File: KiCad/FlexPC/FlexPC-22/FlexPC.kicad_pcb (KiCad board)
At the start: 2 copper layers, 12.7 x 16.6 mm, 3 parts, among them J1 Conn_01x22, J2 Conn_01x20, J3 Conn_01x14

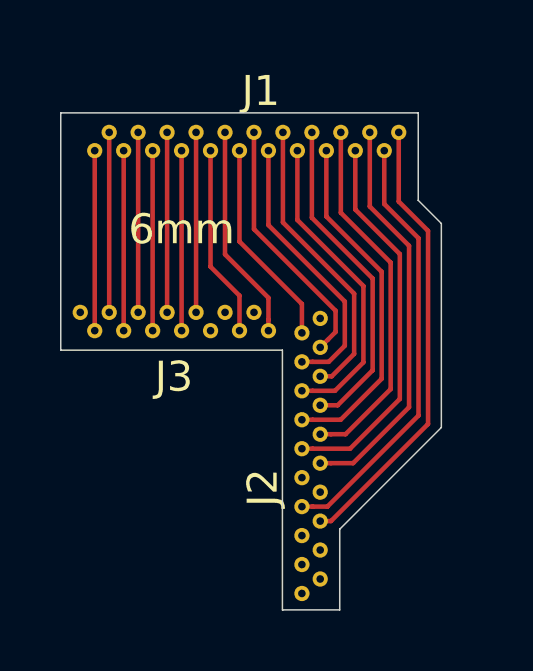
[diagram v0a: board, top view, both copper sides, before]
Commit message: WF Release Board & FlexPC's Updates
1. 23-pin and 3-pin FlexPCs' holes have teardrop shapes now
2. 23-pin flexPC tracks still need to be cleaned up. Not sure how to ensure no curved near the bending area yet.
3. WF board copper planes have been reduced to be 12.5 mils away from the edge cut.
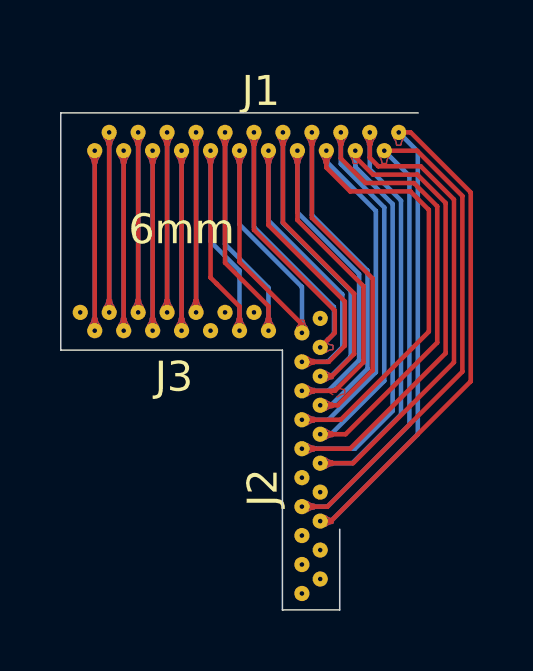
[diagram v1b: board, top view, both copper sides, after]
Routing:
- net /LINE_VALID: track 15.1 -> 31.3 mm
- net /FRAME_VALID: track 14.4 -> 30.5 mm
- net /img_d6: track 13.4 -> 28.7 mm
- net /img_d7: track 12.8 -> 27.7 mm
- net /img_d5: track 12.2 -> 26.2 mm
- net /img_d4: track 11.6 -> 25.3 mm
- net /CLK_OUT: track 11.0 -> 21.7 mm
- net /img_d3: track 10.4 -> 20.6 mm
- net /img_d1: track 9.81 -> 19.5 mm
- net /img_d2: track 9.21 -> 18.3 mm
- net /img_d0: track 8.51 -> 16.9 mm
- net /GND: track 7.21 -> 14.4 mm
- net /1V8: track 6.94 -> 13.9 mm
- net /SS_N: track 6.40 -> 12.8 mm
- net /3V3: track 6.00 -> 12.0 mm
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- added copper zone on B.Cu, net (none)
- added copper zone on F.Cu, net (none)
- added copper zone on B.Cu, net /1V8
- added copper zone on F.Cu, net /1V8
- added copper zone on B.Cu, net /3V3
- added copper zone on F.Cu, net /3V3
- added copper zone on B.Cu, net /CLK_OUT
- added copper zone on F.Cu, net /CLK_OUT
- added copper zone on B.Cu, net /FRAME_VALID
- added copper zone on F.Cu, net /FRAME_VALID
- added copper zone on B.Cu, net /GND
- added copper zone on F.Cu, net /GND
- added copper zone on B.Cu, net /LINE_VALID
- added copper zone on F.Cu, net /LINE_VALID
- added copper zone on B.Cu, net /MISO
- added copper zone on F.Cu, net /MISO
- added copper zone on B.Cu, net /MONITOR0
- added copper zone on F.Cu, net /MONITOR0
- added copper zone on B.Cu, net /MOSI
- added copper zone on F.Cu, net /MOSI
- added copper zone on B.Cu, net /RESET_N
- added copper zone on F.Cu, net /RESET_N
- added copper zone on B.Cu, net /SCK
- added copper zone on F.Cu, net /SCK
- added copper zone on B.Cu, net /SS_N
- added copper zone on F.Cu, net /SS_N
- added copper zone on B.Cu, net /Status_LED
- added copper zone on F.Cu, net /Status_LED
- added copper zone on B.Cu, net /TRIGGER0
- added copper zone on F.Cu, net /TRIGGER0
- added copper zone on B.Cu, net /img_d0
- added copper zone on F.Cu, net /img_d0
- added copper zone on B.Cu, net /img_d1
- added copper zone on F.Cu, net /img_d1
- added copper zone on B.Cu, net /img_d2
- added copper zone on F.Cu, net /img_d2
- added copper zone on B.Cu, net /img_d3
- added copper zone on F.Cu, net /img_d3
- added copper zone on B.Cu, net /img_d4
- added copper zone on F.Cu, net /img_d4
- added copper zone on B.Cu, net /img_d5
- added copper zone on F.Cu, net /img_d5
- added copper zone on B.Cu, net /img_d6
- added copper zone on F.Cu, net /img_d6
- added copper zone on B.Cu, net /img_d7
- added copper zone on F.Cu, net /img_d7
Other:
- board size 12.7 x 16.6 mm -> 11.9 x 16.6 mm
- rule pad_to_mask_clearance: 0.051 -> 0.0254
- rule solder_mask_min_width: 0.25 -> 0.1016
